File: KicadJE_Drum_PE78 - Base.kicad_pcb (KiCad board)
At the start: 2 copper layers, 100 x 100 mm, 194 parts, among them J101 Snare, J102 LCymbals, J103 SCymbals, J104 Maracas, J105 Bass, J106 LBongo, J107 HBongo, J108 Claves, J201 AudioJack2_SwitchT, J202 AudioJack2_SwitchT, J203 AudioJack2_SwitchT, J204 Power +, J205 Power -, J206 Conn_01x03_Male, J207 Conn_01x03_Male, J208 Conn_01x03_Male, J209 Conn_01x03_Male, J210 Conn_01x02_Male, J301 Tone/Noise, J302 RND, J303 Noise, J304 DRUM_OUT, J401 Tone/Noise, P101 HEADER_2x8_Doepfer, P201 HEADER_2x5_Doepfer, P401 HEADER_2x8_Doepfer, Q101 2N3904, Q102 2N3904, Q103 2N3904, Q104 2N3904, SW201 SW_SPDT, U101 74HC04, U302 TL072

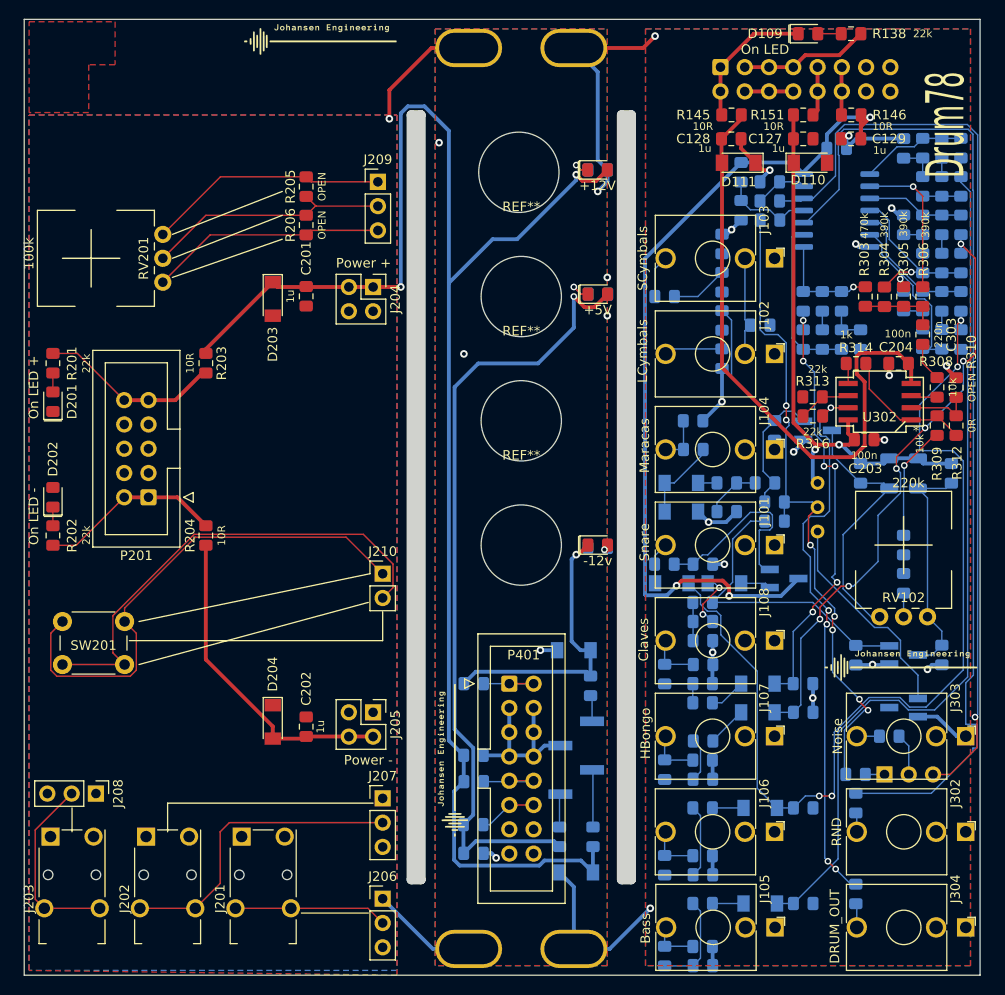
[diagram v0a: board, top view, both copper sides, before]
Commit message: Fix PCB Errors
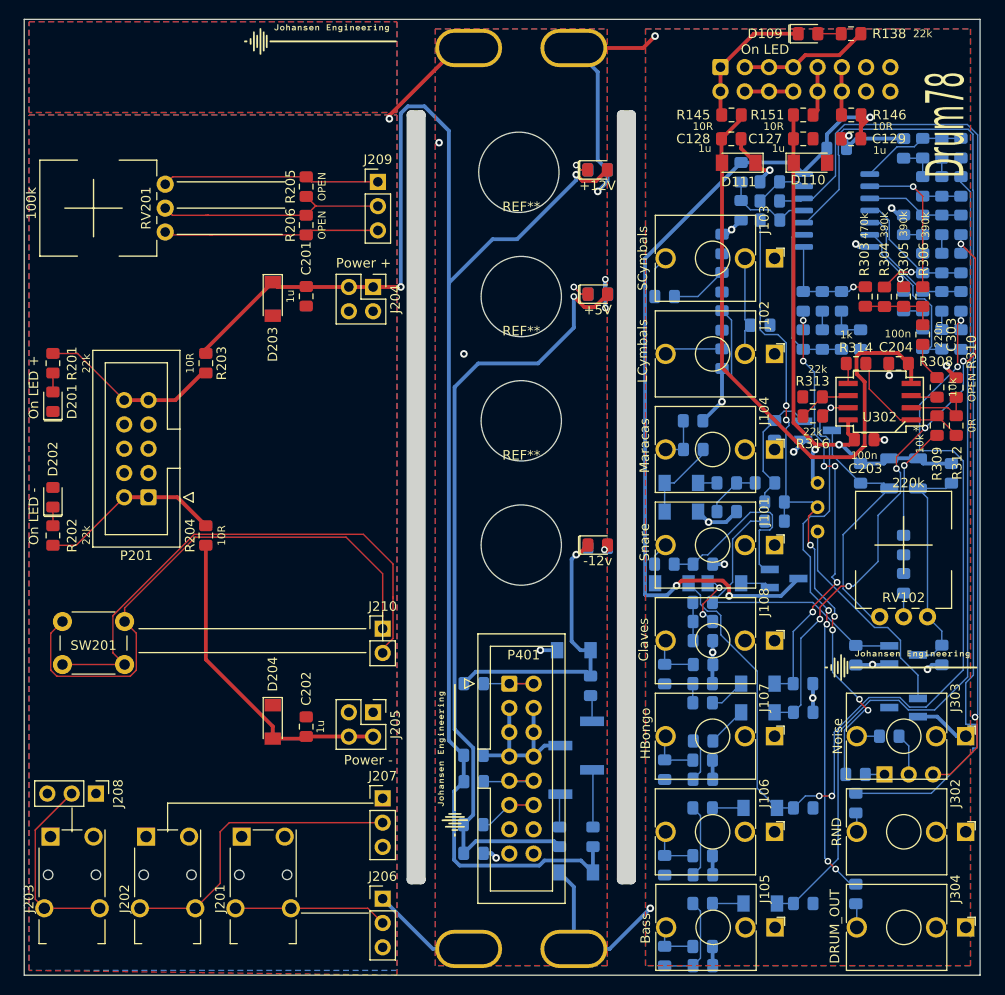
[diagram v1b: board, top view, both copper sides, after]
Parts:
- moved J210 5.75 mm to (87.5, 113.8)
- moved RV201 5.26 mm to (64.8, 67.2)
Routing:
- net Net-(J210-Pad2): track 50.2 -> 56.2 mm
- net Net-(J210-Pad1): track 53.7 -> 59.5 mm
- net GND: track 173.4 -> 176.5 mm, vias 24 -> 26
- net Net-(J209-Pad1): track 25.2 -> 22.8 mm
- net Net-(J209-Pad3): track 24.7 -> 22.8 mm
- net Net-(J209-Pad2): track 26.2 -> 24.6 mm
- net (no net): vias 2 -> 0
- added copper zone on B.Cu, net (none)
